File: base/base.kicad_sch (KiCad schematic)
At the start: 6 parts, among them J1 DF40GB(1.5)-30DS-0.4V(51), J2 DIP-48_Socket

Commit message: wip: snapshot base board before connector/socket rework
Safety commit taken before swapping the mezzanine connector and the
DIP48 socket. No design intent here beyond preserving the tree.

Co-Authored-By: Claude Opus 5 <noreply@anthropic.com>
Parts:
- C1, C2, R1, R2: now not fitted
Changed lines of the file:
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@@
 		(on_board yes)
 		(in_pos_files yes)
-		(dnp no)
+		(dnp yes)
 		(fields_autoplaced yes)
 		(property "Reference" "R1"
@@
 		(on_board yes)
 		(in_pos_files yes)
-		(dnp no)
+		(dnp yes)
 		(fields_autoplaced yes)
 		(property "Reference" "C2"
@@
 		(on_board yes)
 		(in_pos_files yes)
-		(dnp no)
+		(dnp yes)
 		(fields_autoplaced yes)
 		(property "Reference" "R2"
@@
 		(on_board yes)
 		(in_pos_files yes)
-		(dnp no)
+		(dnp yes)
 		(fields_autoplaced yes)
 		(property "Reference" "C1"

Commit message: Swap mezzanine to DF40TC 4.0mm; base DIP48 field goes surface-mount
The 1.5 mm DF40GB stack left no room under the base board and the
through-hole DIP48 socket put tails into the space the carrier occupies.
Both are now addressed by part choice rather than by moving anything.

Mezzanine, 1.5 mm -> 4.0 mm:
  carrier J1  DF40GB-30DP-0.4V(51)     -> DF40TC-30DP-0.4V(51)
  base    J1  DF40GB(1.5)-30DS-0.4V(51)-> DF40TC(4.0)-30DS-0.4V(51)

4.0 mm at 30 positions does not exist in any non-T DF40 family, but it is
mass production in DF40T (125 C, unshielded).  Verified against the
DF40T/DF40GT catalog (Jan 2026) p.2 variation matrix and p.8 combinations
table; 4.5-7.0 mm at 30 pos is still Under Planning, so 4.0 is the ceiling.
The plug carries no stacking height in its part number -- one DF40TC plug
serves 1.5 through 4.0 mm and the receptacle sets the gap.

The land patterns are the reason this is cheap: DF40T catalog p.9 gives the
plug as P=0.4, B=5.60, pad 0.23 wide, rows 3.37/2.05 -> 0.66 long at
y=+-1.355, and DF40 catalog p.10 (DF40HC, No Retention Tab) gives the
receptacle as pad 0.2 x 0.70 at y=+-1.54.  Both are bit-identical to the
DF40GB footprints already in the tree.  All 30 signal pads are unmoved on
both boards; only the four G1-G4 retention/shield tabs go away, because
DF40TC has none.  Verified pad-by-pad against the originals.

Costs of the DF40T family, for the record: 0.3 A instead of 0.5 A (the
flash draws 30 mA), 10 mating cycles instead of 30 (the carrier is the
joint that should stay mated), and no shield.

DIP48 field, through-hole -> surface mount:
  base J2  DIP-48_Socket_W15.24mm_P2.54mm
        -> DIP-48_SocketStrip_SMD_W15.24mm_P2.54mm
Two 1x24 SMT socket strips (Samtec SSM-124-L-SV class) on 15.24 mm
centres.  No one-piece SMT DIP48 at 0.6 in exists in distribution.  Tails
stagger +-1.65 mm about each row centreline, so all 48 pad Y coordinates
are unchanged and the row centres still sit where the adapter pins land;
the inner pad edges leave 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
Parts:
- J1: value DF40GB(1.5)-30DS-0.4V(51) -> DF40TC(4.0)-30DS-0.4V(51); footprint Connector_Hirose_DF40:HIROSE_DF40GB-30DS-0.4V_51_ -> Connector_Hirose_DF40:HIROSE_DF40TC_4.0_-30DS-0.4V_51_; symbol carrier:DF40GB-30DS-0.4V_51_ -> carrier:DF40TC_4.0_-30DS-0.4V_51_
- J2: footprint base:DIP-48_Socket_W15.24mm_P2.54mm -> base:DIP-48_SocketStrip_SMD_W15.24mm_P2.54mm
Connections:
- net GND: no longer J1.G1 (GND), J1.G2 (GND), J1.G3 (GND), J1.G4 (GND)
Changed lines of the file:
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@@
 	)
 	(symbol
-		(lib_id "carrier:DF40GB-30DS-0.4V_51_")
+		(lib_id "carrier:DF40TC_4.0_-30DS-0.4V_51_")
 		(at 63.5 63.5 0)
 		(unit 1)
@@
 			)
 		)
-		(property "Value" "DF40GB(1.5)-30DS-0.4V(51)"
+		(property "Value" "DF40TC(4.0)-30DS-0.4V(51)"
 			(at 63.5 40.64 0)
 			(show_name no)
@@
 			)
 		)
-		(property "Footprint" "Connector_Hirose_DF40:HIROSE_DF40GB-30DS-0.4V_51_"
+		(property "Footprint" "Connector_Hirose_DF40:HIROSE_DF40TC_4.0_-30DS-0.4V_51_"
 			(at 63.5 63.5 0)
 			(hide yes)
@@
 		(pin "30"
 		)
-		(pin "G3"
-		)
 		(pin "23"
 		)
 		(pin "29"
-		)
-		(pin "G2"
 		)
 		(pin "26"
@@
 		(pin "20"
 		)
-		(pin "G1"
-		)
 		(pin "28"
-		)
-		(pin "G4"
 		)
 		(pin "3"
@@
 			)
 		)
-		(property "Footprint" "base:DIP-48_Socket_W15.24mm_P2.54mm"
+		(property "Footprint" "base:DIP-48_SocketStrip_SMD_W15.24mm_P2.54mm"
 			(at 152.4 50.8 0)
 			(hide yes)

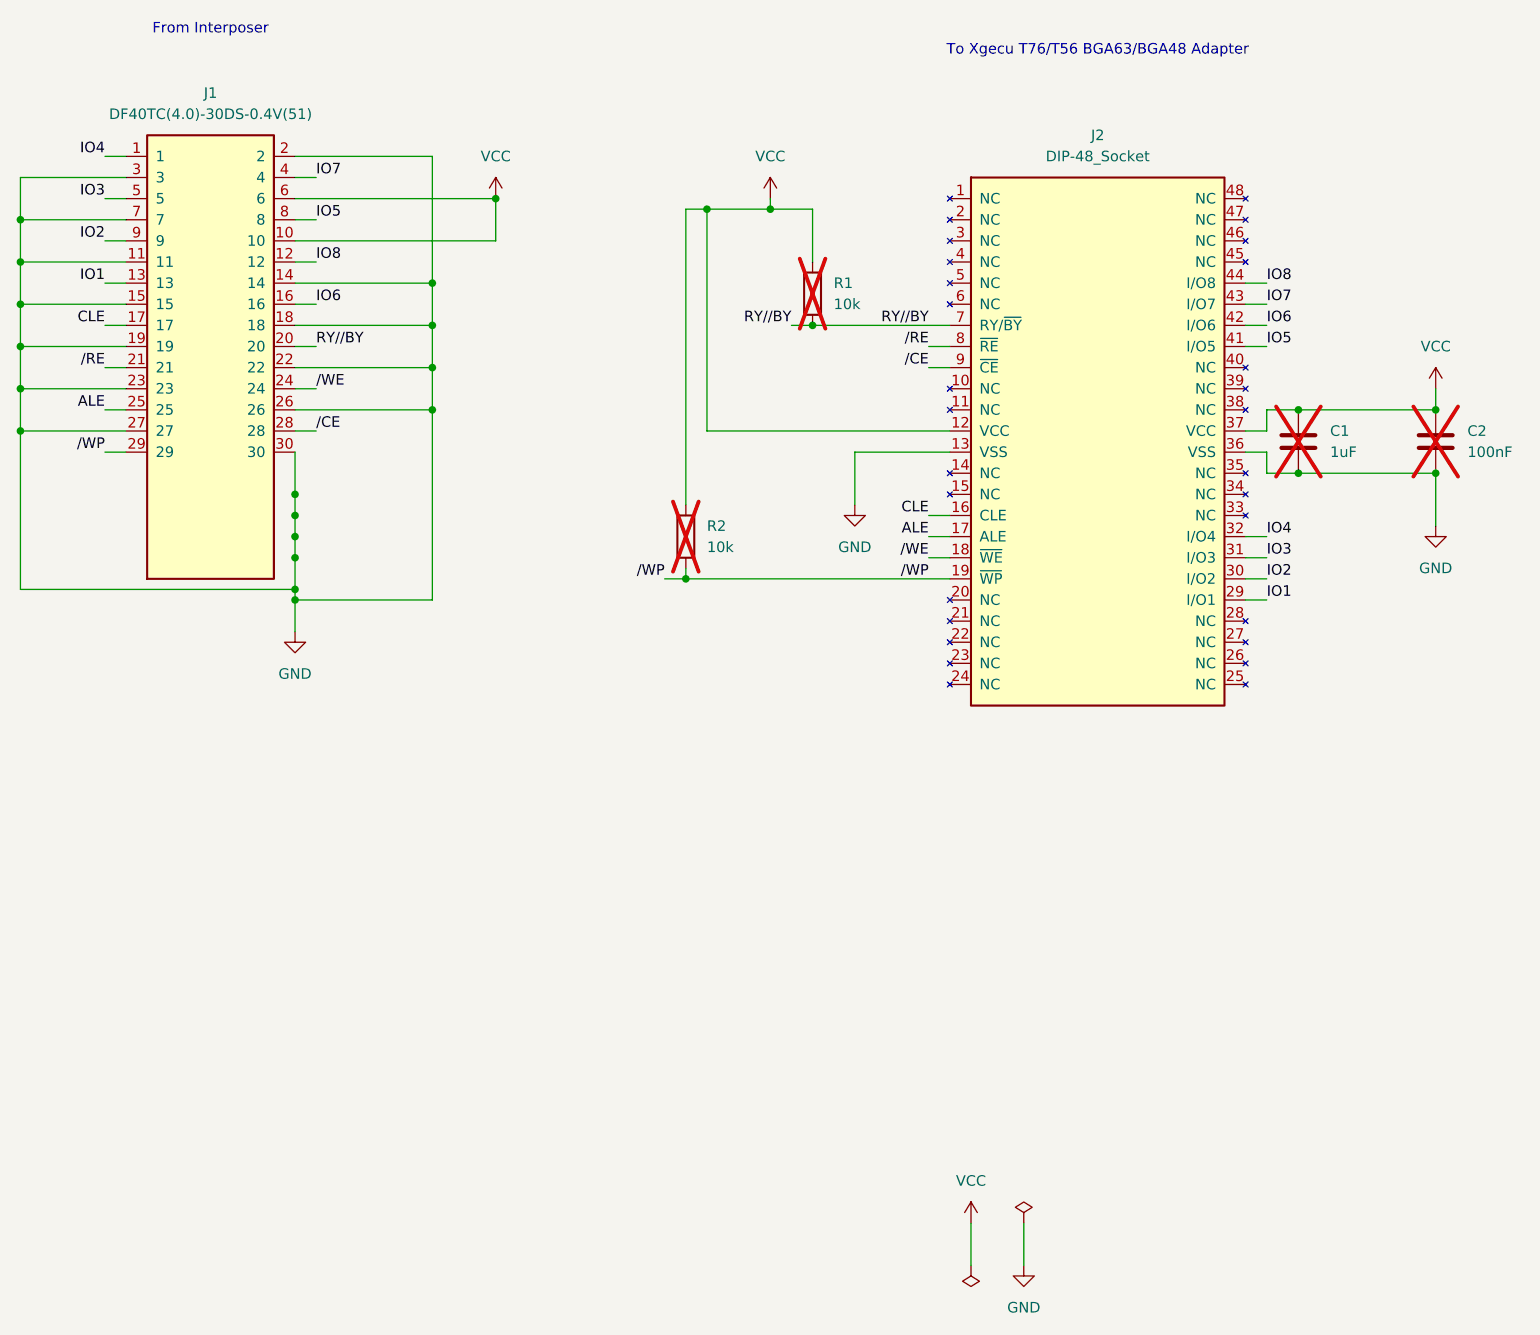
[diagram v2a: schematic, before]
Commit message: Commit routed pinout, checkers, docs and mechanical outputs
Brings the repository up to the state that has been on disk and passing
`make check`: the routed same-number DF40 table replacing the old Courk
DF17-derived pinout, the mating and panel checkers, corrected connector
documentation, JLC rule tooling, and the 3D/mechanical outputs.

Committed as one baseline so the board C and board D work that follows has
reviewable per-task diffs.

Co-Authored-By: Claude Opus 5 <noreply@anthropic.com>
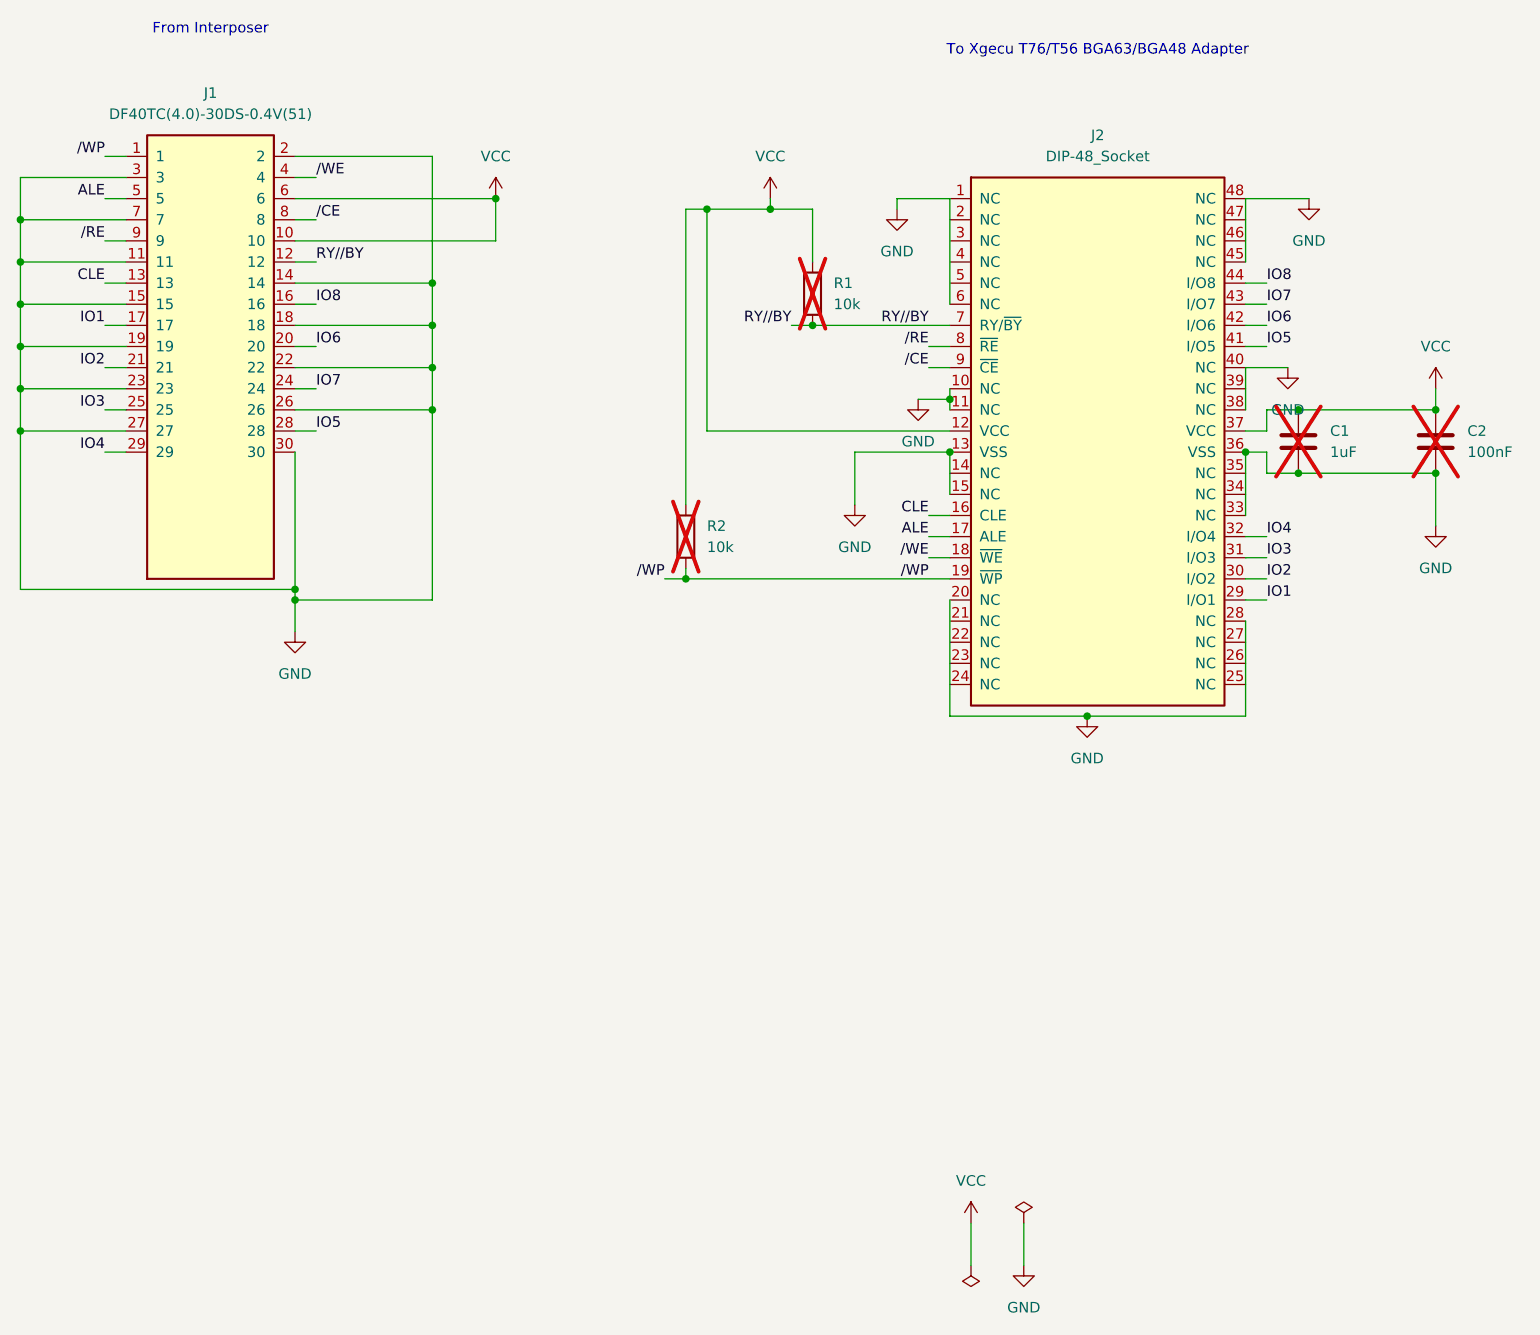
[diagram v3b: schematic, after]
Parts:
- C1, C2, R1, R2: KiLib_Generator (none) -> SMD_2terminal_chip_molded
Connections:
- net ALE: now also J1.5; no longer J1.25
- net CLE: now also J1.13; no longer J1.17
- net GND: now also J2.1 (NC), J2.10 (NC), J2.11 (NC), J2.15 (NC), J2.20 (NC), J2.28 (NC), J2.33 (NC), J2.38 (NC), J2.40 (NC), J2.45 (NC), J2.48 (NC), J2.6 (NC)
- net IO1: now also J1.17; no longer J1.13
- net IO2: now also J1.21; no longer J1.9
- net IO3: now also J1.25; no longer J1.5
- net IO4: now also J1.29; no longer J1.1
- net IO5: now also J1.28; no longer J1.8
- net IO6: now also J1.20; no longer J1.16
- net IO7: now also J1.24; no longer J1.4
- net IO8: now also J1.16; no longer J1.12
- net RY//BY: now also J1.12; no longer J1.20
- net /CE: now also J1.8; no longer J1.28
- net /RE: now also J1.9; no longer J1.21
- net /WE: now also J1.4; no longer J1.24
- net /WP: now also J1.1; no longer J1.29
